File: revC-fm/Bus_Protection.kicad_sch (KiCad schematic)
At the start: 47 parts, among them Q1 BSS138DWQ-7, Q2 BSS138DWQ-7, Q3 MMDT5551-7-F, Q4 MMDT5551-7-F, Q5 BSS138DWQ-7, Q6 BSS138DWQ-7, Q7 MMDT5551-7-F, Q8 MMDT5551-7-F, Q9 MMDT2907AQ-7-F

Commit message: working revC
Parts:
- renumbered C38 to C27, C40 to C28, C39 to C29, C41 to C30, Q6 to Q10, Q9 to Q2, Q7 to Q4, Q1 to Q5, Q5 to Q6, Q4 to Q7, Q2 to Q9, R82 to R24, R80 to R25, R56 to R26, R70 to R27, R78 to R28, R83 to R29, R58 to R30, R72 to R31, R53 to R32, R67 to R33, R84 to R34, R81 to R35, R52 to R36, R66 to R37, R59 to R38, R73 to R39, R79 to R40, R85 to R41, R57 to R42, R71 to R43, R60 to R44, R74 to R45, R55 to R46, R69 to R47, R54 to R48, R68 to R49, R61 to R50, R75 to R51, R62 to R52, R63 to R53, R76 to R54, R64 to R55, R77 to R56, R65 to R57
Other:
- note removed: "sub'd q15, 16 was MBR2222ADW1T1"
- note removed: "sub'd q7,8 was MBR2222ADW1T1"

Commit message: working revC
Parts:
- added C78, C79: 10nF, Capacitor_SMD:C_0603_1608Metric, symbol Device:C
- added Q23, Q24: MMDT5551-7-F, Package_TO_SOT_SMD:SOT-363_SC-70-6, symbol Transistor_BJT:MMDT5551
- added Q27, Q28: BSS138DWQ-7, Package_TO_SOT_SMD:SOT-363_SC-70-6, symbol SierraLobo:BSS138DW
- added R137, R138, R143, R144: 10k, Resistor_SMD:R_0603_1608Metric, symbol Device:R_US
- added R147, R148: 680, Resistor_SMD:R_0603_1608Metric, symbol Device:R_US
- added R153, R154: 100k, Resistor_SMD:R_0603_1608Metric, symbol Device:R_US
- added R157, R158: 200k, Resistor_SMD:R_0603_1608Metric, symbol Device:R_US
- added R172, R174: 0, Resistor_SMD:R_0603_1608Metric, symbol Device:R_US
- Q20: renamed from Q2; symbol mainboard:MMDT2907 -> SierraLobo:MMDT2907; Flight MMDT2907AQ-7-F -> (none); Manufacturer_Name Diodes Incorporated -> (none); Manufacturer_Part_Number MMDT2907AQ-7-F -> (none); Proto MMDT2907A -> (none)
- Q21: renamed from Q3; symbol mainboard-rescue:MBT2222ADW1T1-Transistor_BJT-mainboard-rescue -> Transistor_BJT:MMDT5551
- Q21: renamed from Q3; symbol mainboard-rescue:MBT2222ADW1T1-Transistor_BJT-mainboard-rescue -> Transistor_BJT:MMDT5551; Flight MMDT5551-7-F -> (none)
- Q22: renamed from Q4; symbol mainboard-rescue:MBT2222ADW1T1-Transistor_BJT-mainboard-rescue -> Transistor_BJT:MMDT5551; Flight MBT2222ADW1T1G -> (none); Manufacturer_Name ON Semiconductor -> (none); Manufacturer_Part_Number MBT2222ADW1T1G -> (none); Proto MBT2222ADW1T1G -> (none)
- Q22: renamed from Q4; symbol mainboard-rescue:MBT2222ADW1T1-Transistor_BJT-mainboard-rescue -> Transistor_BJT:MMDT5551; Flight MMDT5551-7-F -> (none)
- Q25: renamed from Q5; footprint mainboard:BSS138DWQ-7 -> Package_TO_SOT_SMD:SOT-363_SC-70-6; symbol mainboard:BSS138DWQ-7 -> SierraLobo:BSS138DW; Flight BSS138DWQ-7 -> (none); Manufacturer_Name Diodes Incorporated -> (none); Manufacturer_Part_Number BSS138DWQ-7 -> (none); Proto BSS138DWQ-7 -> (none)
- Q26: renamed from Q6; footprint mainboard:BSS138DWQ-7 -> Package_TO_SOT_SMD:SOT-363_SC-70-6; symbol mainboard:BSS138DWQ-7 -> SierraLobo:BSS138DW; Flight BSS138DWQ-7 -> (none); Manufacturer_Name Diodes Incorporated -> (none); Manufacturer_Part_Number BSS138DWQ-7 -> (none); Proto BSS138DWQ-7 -> (none)
- Q29: renamed from Q7; symbol mainboard-rescue:MBT2222ADW1T1-Transistor_BJT-mainboard-rescue -> Transistor_BJT:MMDT5551; Flight MMDT5551-7-F -> (none)
- Q29: renamed from Q7; symbol mainboard-rescue:MBT2222ADW1T1-Transistor_BJT-mainboard-rescue -> Transistor_BJT:MMDT5551; Flight MBT2222ADW1T1G -> (none); Manufacturer_Name ON Semiconductor -> (none); Manufacturer_Part_Number MBT2222ADW1T1G -> (none); Proto MBT2222ADW1T1G -> (none)
- Q30: renamed from Q8; symbol mainboard-rescue:MBT2222ADW1T1-Transistor_BJT-mainboard-rescue -> Transistor_BJT:MMDT5551; Flight MMDT5551-7-F -> (none)
- Q30: renamed from Q8; symbol mainboard-rescue:MBT2222ADW1T1-Transistor_BJT-mainboard-rescue -> Transistor_BJT:MMDT5551; Flight MBT2222ADW1T1G -> (none); Manufacturer_Name ON Semiconductor -> (none); Manufacturer_Part_Number MBT2222ADW1T1G -> (none); Proto MBT2222ADW1T1G -> (none)
- Q31: renamed from Q9; footprint mainboard:BSS138DWQ-7 -> Package_TO_SOT_SMD:SOT-363_SC-70-6; symbol mainboard:BSS138DWQ-7 -> SierraLobo:BSS138DW; Flight BSS138DWQ-7 -> (none); Manufacturer_Name Diodes Incorporated -> (none); Manufacturer_Part_Number BSS138DWQ-7 -> (none); Proto BSS138DWQ-7 -> (none)
- Q32: renamed from Q10; footprint mainboard:BSS138DWQ-7 -> Package_TO_SOT_SMD:SOT-363_SC-70-6; symbol mainboard:BSS138DWQ-7 -> SierraLobo:BSS138DW; Flight BSS138DWQ-7 -> (none); Manufacturer_Name Diodes Incorporated -> (none); Manufacturer_Part_Number BSS138DWQ-7 -> (none); Proto BSS138DWQ-7 -> (none)
- R171: renamed from R52; DNI DNI -> (none); now not fitted
- R173: renamed from R53; DNI DNI -> (none); now not fitted
- R175: renamed from R54; DNI DNI -> (none); now not fitted
- R176: renamed from R55; DNI DNI -> (none); now not fitted
- R177: renamed from R56; DNI DNI -> (none); now not fitted
- R178: renamed from R57; DNI DNI -> (none); now not fitted
- renumbered C27 to C76, C28 to C77, C29 to C80, C30 to C81, R24 to R133, R25 to R134, R26 to R135, R27 to R136, R28 to R139, R29 to R140, R30 to R141, R31 to R142, R32 to R145, R33 to R146, R34 to R149, R35 to R150, R36 to R151, R37 to R152, R38 to R155, R39 to R156, R40 to R159, R41 to R160, R42 to R161, R43 to R162, R44 to R163, R45 to R164, R46 to R165, R47 to R166, R48 to R167, R49 to R168, R50 to R169, R51 to R170
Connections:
- net 3.3V: now also R137.1, R138.1, R143.1, R144.1, R153.1, R154.1
- net GND: now also C78.2, C79.2, Q27.1 (S2), Q27.4 (S1), Q28.1 (S2), Q28.4 (S1)
- net SCL: now also Q23.1 (E1), Q23.3 (C2), R172.2
- net SDA: now also Q24.1 (E1), Q24.3 (C2), R174.2
- new net: C79.1, Q28.5 (G1), R158.2
- new net: Q23.2 (B1), R147.1
- new net: Q23.5 (B2), Q27.6 (D1), R137.2, R147.2
- new net: Q24.2 (B1), R148.1
- new net: Q24.5 (B2), Q28.6 (D1), R138.2, R148.2
- new net: Q27.2 (G2), Q27.3 (D2), R153.2
- new net: C78.1, Q27.5 (G1), R157.2
- new net: Q28.2 (G2), Q28.3 (D2), R154.2
- new net SCL_BUS: Q23.4 (E2), Q23.6 (C1), R143.2, R157.1, R172.1
- new net SDA_BUS: Q24.4 (E2), Q24.6 (C1), R144.2, R158.1, R174.1
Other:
- note added: "I2C Bus Protection - Mainboard to Bus"

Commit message: routing fm
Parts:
- added Q52: MMDT2907AQ-7-F, Package_TO_SOT_SMD:SOT-363_SC-70-6, symbol SierraLobo:MMDT2907
- added R219, R229: 1k, Resistor_SMD:R_0603_1608Metric, symbol Device:R_US
- added R224: 4.7k, Resistor_SMD:R_0603_1608Metric, symbol Device:R_US
- added R225, R231: 0, Resistor_SMD:R_0603_1608Metric, symbol Device:R_US
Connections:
- net MISO: now also Q52.6 (C1), R231.2
- net MOSI: now also R229.1
- net SCK: now also R219.2
- net at R139.1: now also Q52.1 (E1); no longer Q20.4 (E2)
- net at R134.1: now also Q52.2 (B1); no longer Q20.5 (B2)
- new net: Q20.4 (E2), R225.1
- new net: Q20.5 (B2), R224.1
- new net MISO_RF2: R225.2, R231.1
- new net MOSI_RF2: R229.2
- new net RF2_CS: R224.2
- new net SCK_RF2: R219.1
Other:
- note added: "SPI Bus Protection - Radio 2"
- moved on the sheet: Q20B, R172, R174, R175, R177

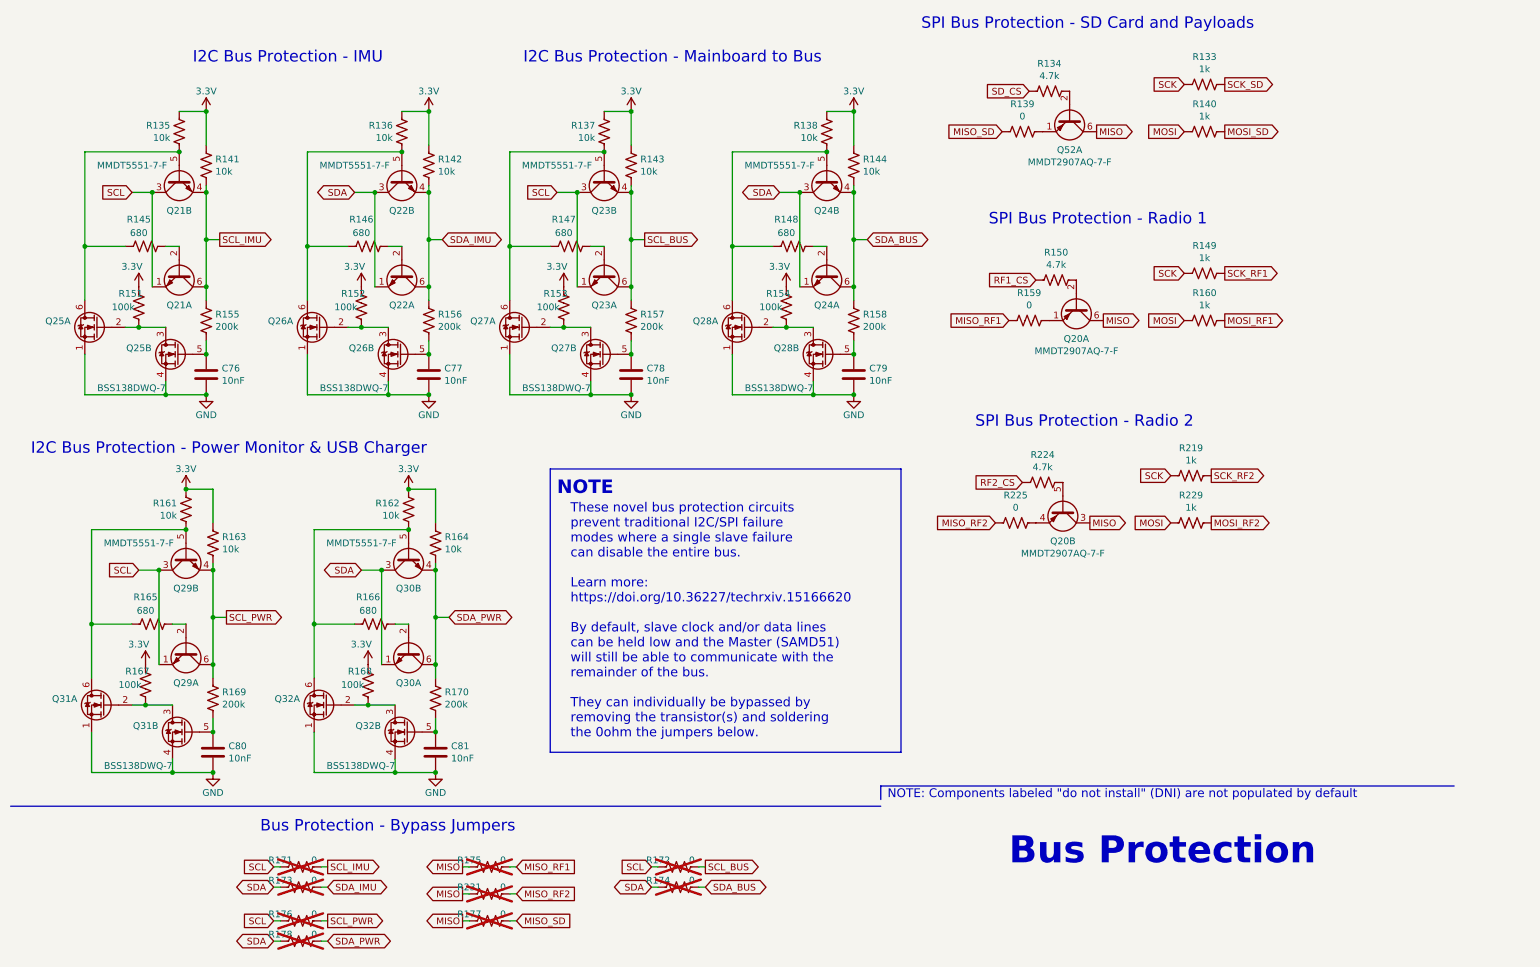
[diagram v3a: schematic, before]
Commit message: updated analog , solar comp, layout
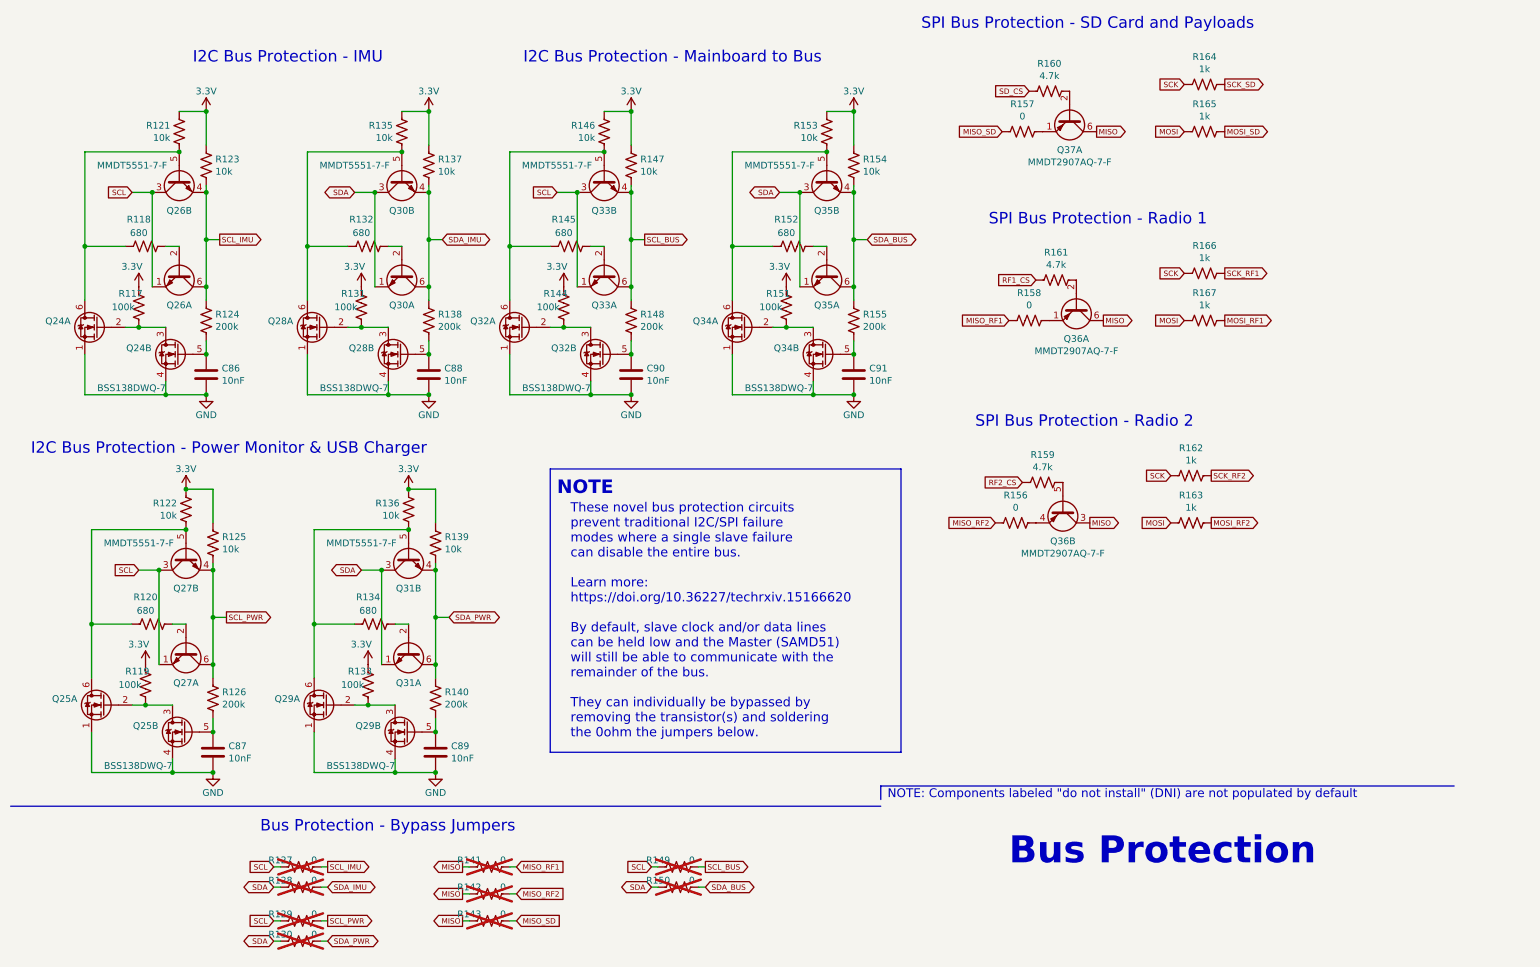
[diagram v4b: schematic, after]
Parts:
- C86: renamed from C76; footprint Capacitor_SMD:C_0603_1608Metric -> Capacitor_SMD:C_0402_1005Metric
- C87: renamed from C80; footprint Capacitor_SMD:C_0603_1608Metric -> Capacitor_SMD:C_0402_1005Metric
- C88: renamed from C77; footprint Capacitor_SMD:C_0603_1608Metric -> Capacitor_SMD:C_0402_1005Metric
- C89: renamed from C81; footprint Capacitor_SMD:C_0603_1608Metric -> Capacitor_SMD:C_0402_1005Metric
- C90: renamed from C78; footprint Capacitor_SMD:C_0603_1608Metric -> Capacitor_SMD:C_0402_1005Metric
- C91: renamed from C79; footprint Capacitor_SMD:C_0603_1608Metric -> Capacitor_SMD:C_0402_1005Metric
- renumbered Q25 to Q24, Q31 to Q25, Q21 to Q26, Q29 to Q27, Q26 to Q28, Q32 to Q29, Q22 to Q30, Q30 to Q31, Q27 to Q32, Q23 to Q33, Q28 to Q34, Q24 to Q35, Q20 to Q36, Q52 to Q37, R151 to R117, R145 to R118, R167 to R119, R165 to R120, R135 to R121, R161 to R122, R141 to R123, R155 to R124, R163 to R125, R169 to R126, R171 to R127, R173 to R128, R176 to R129, R178 to R130, R152 to R131, R146 to R132, R168 to R133, R166 to R134, R136 to R135, R162 to R136, R142 to R137, R156 to R138, R164 to R139, R170 to R140, R175 to R141, R231 to R142, R177 to R143, R153 to R144, R147 to R145, R137 to R146, R143 to R147, R157 to R148, R172 to R149, R174 to R150, R154 to R151, R148 to R152, R138 to R153, R144 to R154, R158 to R155, R225 to R156, R139 to R157, R159 to R158, R224 to R159, R134 to R160, R150 to R161, R219 to R162, R229 to R163, R133 to R164, R140 to R165, R149 to R166, R160 to R167

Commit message: routing
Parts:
- C91: renamed from C86; footprint Capacitor_SMD:C_0402_1005Metric -> Capacitor_SMD:C_0603_1608Metric
- C92: renamed from C88; footprint Capacitor_SMD:C_0402_1005Metric -> Capacitor_SMD:C_0603_1608Metric
- C93: renamed from C90; footprint Capacitor_SMD:C_0402_1005Metric -> Capacitor_SMD:C_0603_1608Metric
- C94: renamed from C91; footprint Capacitor_SMD:C_0402_1005Metric -> Capacitor_SMD:C_0603_1608Metric
- C95: renamed from C87; footprint Capacitor_SMD:C_0402_1005Metric -> Capacitor_SMD:C_0603_1608Metric
- C96: renamed from C89; footprint Capacitor_SMD:C_0402_1005Metric -> Capacitor_SMD:C_0603_1608Metric
- renumbered Q37 to Q24, Q26 to Q25, Q30 to Q26, Q33 to Q27, Q35 to Q28, Q36 to Q29, Q24 to Q30, Q28 to Q31, Q34 to Q33, Q27 to Q34, Q31 to Q35, Q25 to Q36, Q29 to Q37, R164 to R104, R160 to R105, R121 to R106, R135 to R107, R146 to R108, R153 to R109, R157 to R110, R165 to R111, R123 to R112, R137 to R113, R147 to R114, R154 to R115, R118 to R116, R132 to R117, R145 to R118, R152 to R119, R166 to R120, R161 to R121, R117 to R122, R131 to R123, R144 to R124, R151 to R125, R124 to R126, R138 to R127, R148 to R128, R155 to R129, R158 to R130, R167 to R131, R162 to R132, R159 to R133, R122 to R134, R136 to R135, R156 to R136, R163 to R137, R125 to R138, R120 to R140, R134 to R141, R119 to R142, R133 to R143, R126 to R144, R140 to R145, R127 to R146, R141 to R147, R149 to R148, R128 to R149, R142 to R151, R129 to R152, R143 to R153, R130 to R154

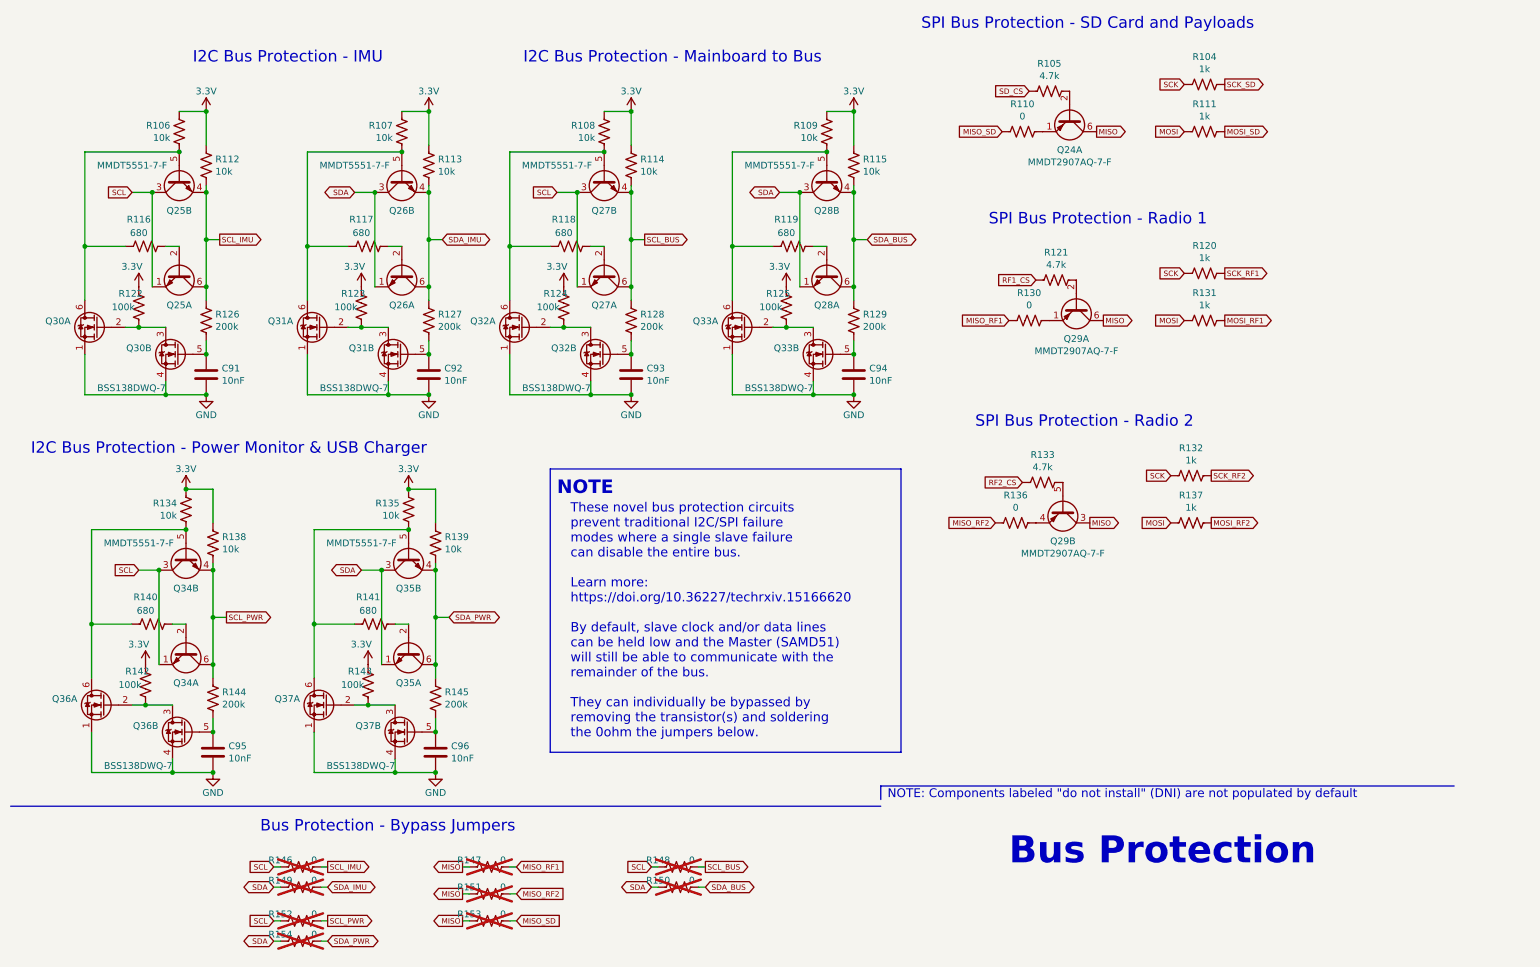
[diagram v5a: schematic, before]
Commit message: changed RF connector to TH
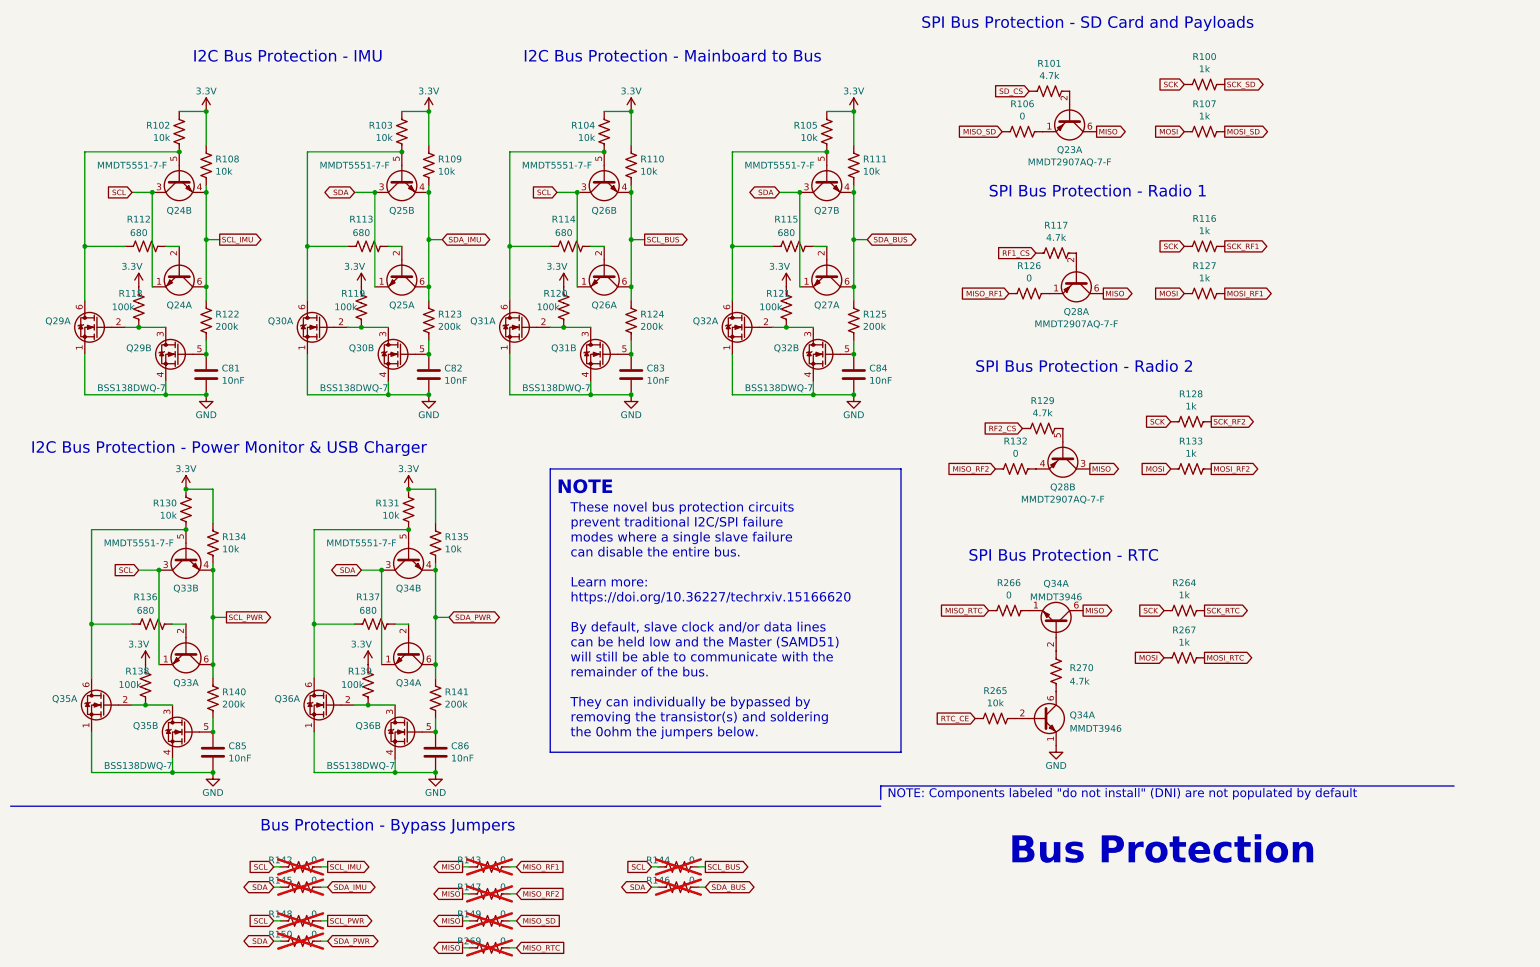
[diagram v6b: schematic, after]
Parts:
- added Q34 (x2): MMDT3946, Package_TO_SOT_SMD:SOT-363_SC-70-6, symbol Transistor_BJT:MMDT3946
- added R264, R267: 1k, Resistor_SMD:R_0603_1608Metric, symbol Device:R_US
- added R265: 10k, Resistor_SMD:R_0603_1608Metric, symbol Device:R_US
- added R266, R269: 0, Resistor_SMD:R_0603_1608Metric, symbol Device:R_US
- added R270: 4.7k, Resistor_SMD:R_0603_1608Metric, symbol Device:R_US
- renumbered C91 to C81, C92 to C82, C93 to C83, C94 to C84, C95 to C85, C96 to C86, Q24 to Q23, Q25 to Q24, Q26 to Q25, Q27 to Q26, Q28 to Q27, Q29 to Q28, Q30 to Q29, Q31 to Q30, Q32 to Q31, Q33 to Q32, Q34 to Q33, Q35 to Q34, Q36 to Q35, Q37 to Q36, R104 to R100, R105 to R101, R106 to R102, R107 to R103, R108 to R104, R109 to R105, R110 to R106, R111 to R107, R112 to R108, R113 to R109, R114 to R110, R115 to R111, R116 to R112, R117 to R113, R118 to R114, R119 to R115, R120 to R116, R121 to R117, R122 to R118, R123 to R119, R124 to R120, R125 to R121, R126 to R122, R127 to R123, R128 to R124, R129 to R125, R130 to R126, R131 to R127, R132 to R128, R133 to R129, R134 to R130, R135 to R131, R136 to R132, R137 to R133, R138 to R134, R139 to R135, R140 to R136, R141 to R137, R142 to R138, R143 to R139, R144 to R140, R145 to R141, R146 to R142, R147 to R143, R148 to R144, R149 to R145, R150 to R146, R151 to R147, R152 to R148, R153 to R149, R154 to R150
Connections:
- net GND: now also Q34.1 (E1)
- net MISO: now also Q34.6 (C1), R269.2
- net MOSI: now also R267.1
- net SCK: now also R264.2
- new net: Q34.2 (B1), R265.1
- new net: Q34.6 (C1), R270.2
- new net: Q34.1 (E1), R266.1
- new net: Q34.2 (B1), R270.1
- new net MISO_RTC: R266.2, R269.1
- new net MOSI_RTC: R267.2
- new net RTC_CE: R265.2
- new net SCK_RTC: R264.1
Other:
- note added: "SPI Bus Protection - RTC"
- moved on the sheet: Q28A, Q28B, R116, R117, R126, R127, R128, R129, R132, R133

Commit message: working revC review changes
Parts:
- renumbered C81 to C82, C82 to C83, C83 to C84, C84 to C85, C85 to C86, C86 to C87, Q23 to Q24, Q24 to Q25, Q25 to Q26, Q26 to Q27, Q27 to Q28, Q28 to Q29, Q29 to Q30, Q30 to Q31, Q31 to Q32, Q32 to Q33, Q33 to Q34, Q34 to Q35, Q35 to Q37, Q36 to Q38, R100 to R106, R101 to R107, R102 to R108, R103 to R109, R104 to R110, R105 to R111, R106 to R112, R107 to R113, R108 to R114, R109 to R115, R110 to R116, R111 to R117, R112 to R118, R113 to R119, R114 to R120, R115 to R121, R116 to R122, R117 to R123, R126 to R124, R127 to R125, R118 to R126, R119 to R127, R120 to R128, R121 to R129, R122 to R130, R123 to R131, R124 to R132, R125 to R133, R128 to R134, R129 to R135, R132 to R136, R133 to R137, R130 to R138, R131 to R139, R134 to R140, R135 to R141, R266 to R142, R264 to R143, R136 to R144, R137 to R145, R267 to R146, R270 to R147, R138 to R148, R139 to R149, R140 to R150, R141 to R151, R265 to R152, R142 to R153, R143 to R154, R144 to R155, R145 to R156, R146 to R157, R147 to R158, R148 to R159, R149 to R160, R150 to R161, R269 to R162
